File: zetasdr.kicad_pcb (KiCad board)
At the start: 2 copper layers, 67 x 92 mm, 61 parts, among them J1 USB_B, J2 Input AWG, J3 Conn_02x02_Counter_Clockwise, J4 Output I, J5 Output Q, J6 Antenna, J7 Conn_02x02_Counter_Clockwise, J8 Conn_02x02_Counter_Clockwise, Q1 BC547C, U1 74HC74, U2 74AHC1G04, U3 4052, U4 NE5532

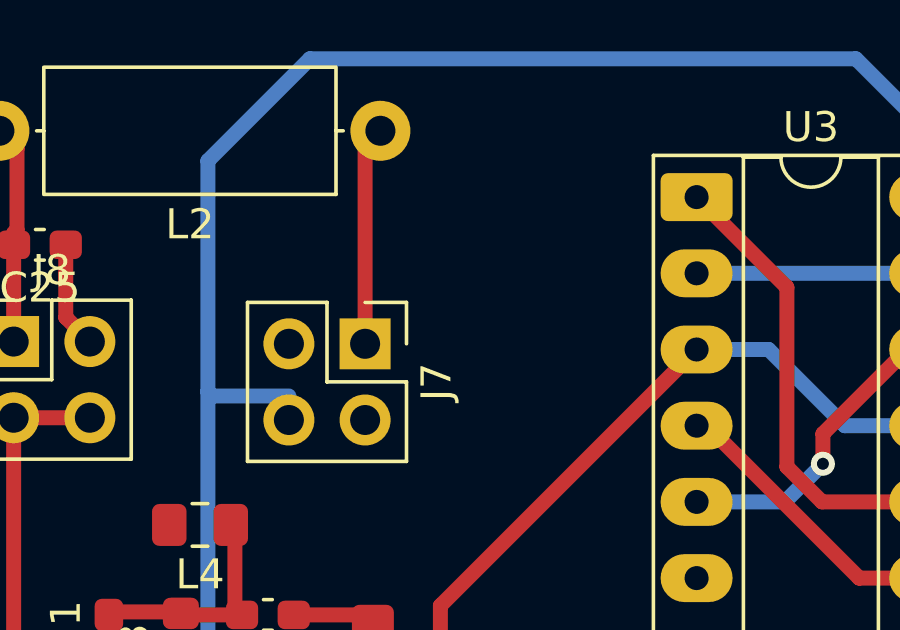
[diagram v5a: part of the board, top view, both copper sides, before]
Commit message: bias tee power filter
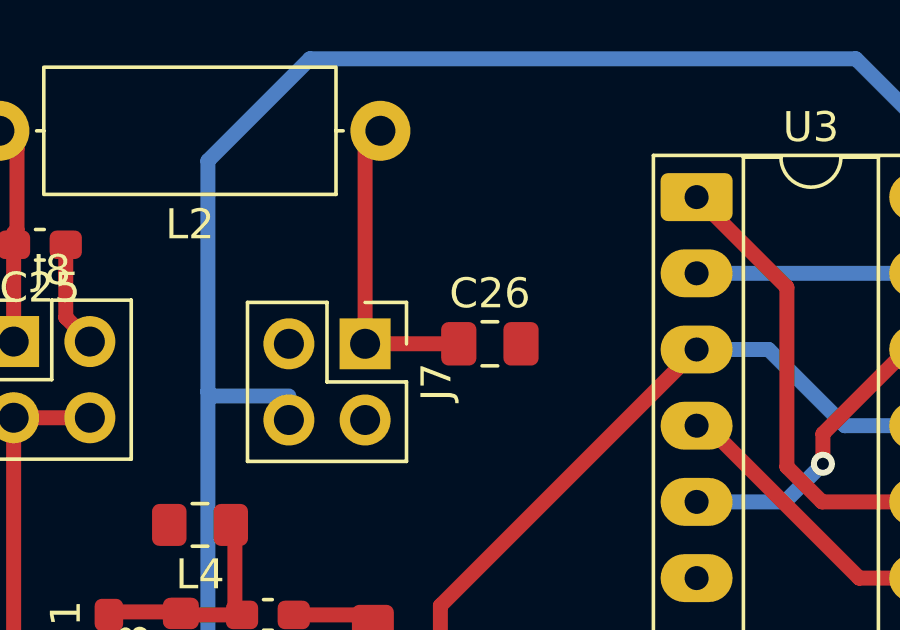
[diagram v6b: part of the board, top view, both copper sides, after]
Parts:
- added C26: 100n, Capacitor_SMD:C_0805_2012Metric_Pad1.18x1.45mm_HandSolder, F.Cu at (160.9, 54.0)
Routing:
- net Net-(J7-Pin_1): track 7.31 -> 10.4 mm
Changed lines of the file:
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@@
 			)
 		)
+		(property "RET" "SMCC-220K-02"
+			(at 0 0 180)
+			(unlocked yes)
+			(layer "F.Fab")
+			(hide yes)
+			(effects
+				(font
+					(size 1 1)
+					(thickness 0.15)
+				)
+			)
+		)
 		(property ki_fp_filters "Choke_* *Coil* Inductor_* L_*")
 		(sheetname "/")
@@
 		)
 	)
+	(footprint "Capacitor_SMD:C_0805_2012Metric_Pad1.18x1.45mm_HandSolder"
+		(layer "F.Cu")
+		(at 160.9 54)
+		(descr "Capacitor SMD 0805 (2012 Metric), square (rectangular) end terminal, IPC-7351 nominal with elongated pad for handsoldering. (Body size source: IPC-SM-782 page 76, https://www.pcb-3d.com/wordpress/wp-content/uploads/ipc-sm-782a_amendment_1_and_2.pdf, https://docs.google.com/spreadsheets/d/1BsfQQcO9C6DZCsRaXUlFlo91Tg2WpOkGARC1WS5S8t0/edit?usp=sharing), generated with kicad-footprint-generator")
+		(tags "capacitor handsolder")
+		(property "Reference" "C26"
+			(at 0 -1.68 0)
+			(layer "F.SilkS")
+			(effects
+				(font
+					(size 1 1)
+					(thickness 0.15)
+				)
+			)
+		)
+		(property "Value" "100n"
+			(at 0 1.68 0)
+			(layer "F.Fab")
+			(effects
+				(font
+					(size 1 1)
+					(thickness 0.15)
+				)
+			)
+		)
+		(property "Datasheet" ""
+			(at 0 0 0)
+			(layer "F.Fab")
+			(hide yes)
+			(effects
+				(font
+					(size 1.27 1.27)
+					(thickness 0.15)
+				)
+			)
+		)
+		(property "Description" "Unpolarized capacitor"
+			(at 0 0 0)
+			(layer "F.Fab")
+			(hide yes)
+			(effects
+				(font
+					(size 1.27 1.27)
+					(thickness 0.15)
+				)
+			)
+		)
+		(property ki_fp_filters "C_*")
+		(sheetname "/")
+		(sheetfile "zetasdr.kicad_sch")
+		(attr smd)
+		(fp_line
+			(start -0.261252 -0.735)
+			(end 0.261252 -0.735)
+			(stroke
+				(width 0.12)
+				(type solid)
+			)
+			(layer "F.SilkS")
+		)
+		(fp_line
+			(start -0.261252 0.735)
+			(end 0.261252 0.735)
+			(stroke
+				(width 0.12)
+				(type solid)
+			)
+			(layer "F.SilkS")
+		)
+		(fp_line
+			(start -1.88 -0.98)
+			(end 1.88 -0.98)
+			(stroke
+				(width 0.05)
+				(type solid)
+			)
+			(layer "F.CrtYd")
+		)
+		(fp_line
+			(start -1.88 0.98)
+			(end -1.88 -0.98)
+			(stroke
+				(width 0.05)
+				(type solid)
+			)
+			(layer "F.CrtYd")
+		)
+		(fp_line
+			(start 1.88 -0.98)
+			(end 1.88 0.98)
+			(stroke
+				(width 0.05)
+				(type solid)
+			)
+			(layer "F.CrtYd")
+		)
+		(fp_line
+			(start 1.88 0.98)
+			(end -1.88 0.98)
+			(stroke
+				(width 0.05)
+				(type solid)
+			)
+			(layer "F.CrtYd")
+		)
+		(fp_line
+			(start -1 -0.625)
+			(end 1 -0.625)
+			(stroke
+				(width 0.1)
+				(type solid)
+			)
+			(layer "F.Fab")
+		)
+		(fp_line
+			(start -1 0.625)
+			(end -1 -0.625)
+			(stroke
+				(width 0.1)
+				(type solid)
+			)
+			(layer "F.Fab")
+		)
+		(fp_line
+			(start 1 -0.625)
+			(end 1 0.625)
+			(stroke
+				(width 0.1)
+				(type solid)
+			)
+			(layer "F.Fab")
+		)
+		(fp_line
+			(start 1 0.625)
+			(end -1 0.625)
+			(stroke
+				(width 0.1)
+				(type solid)
+			)
+			(layer "F.Fab")
+		)
+		(fp_text user "${REFERENCE}"
+			(at 0 0 0)
+			(layer "F.Fab")
+			(effects
+				(font
+					(size 0.5 0.5)
+					(thickness 0.08)
+				)
+			)
+		)
+		(pad "1" smd roundrect
+			(at -1.0375 0)
+			(size 1.175 1.45)
+			(layers "F.Cu" "F.Mask" "F.Paste")
+			(roundrect_rratio 0.212766)
+			(net 33 "Net-(J7-Pin_1)")
+			(pintype "passive")
+		)
+		(pad "2" smd roundrect
+			(at 1.0375 0)
+			(size 1.175 1.45)
+			(layers "F.Cu" "F.Mask" "F.Paste")
+			(roundrect_rratio 0.212766)
+			(net 1 "GND")
+			(pintype "passive")
+		)
+		(embedded_fonts no)
+		(model "${KICAD9_3DMODEL_DIR}/Capacitor_SMD.3dshapes/C_0805_2012Metric.step"
+			(offset
+				(xyz 0 0 0)
+			)
+			(scale
+				(xyz 1 1 1)
+			)
+			(rotate
+				(xyz 0 0 0)
+			)
+		)
+	)
 	(footprint "Resistor_SMD:R_0805_2012Metric_Pad1.20x1.40mm_HandSolder"
 		(layer "F.Cu")
@@
 	)
 	(segment
+		(start 159.8625 54)
+		(end 156.74 54)
+		(width 0.5)
+		(layer "F.Cu")
+		(net 33)
+	)
+	(segment
